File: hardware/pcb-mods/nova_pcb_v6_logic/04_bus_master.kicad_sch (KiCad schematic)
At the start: 5 parts, among them J9 FE-URT-1, U6 Teensy4.1, U7 74HC125

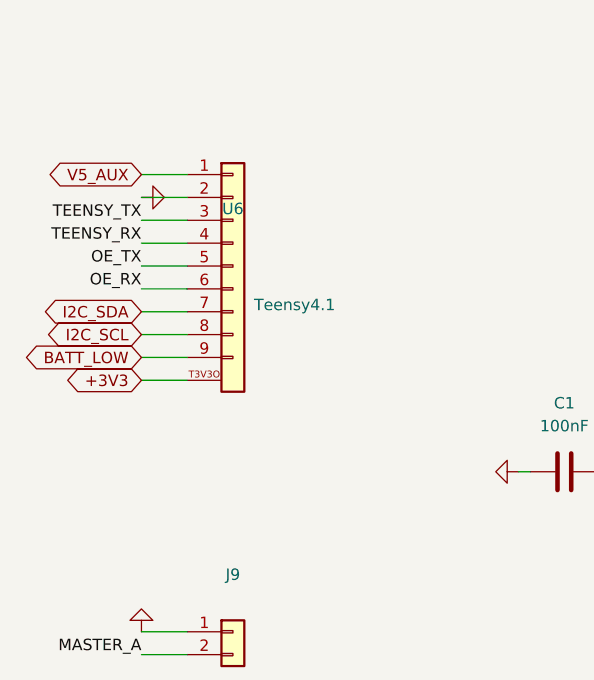
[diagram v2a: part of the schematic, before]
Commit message: logic board: add e-stop sense to Teensy + reconcile firmware pins to board
Hardware e-stop (Q3) killed bucks autonomously but the Teensy was blind —
no ESTOP line crossed J20 (all 12 pins used). Added direct sense so the
SafetyFSM, /estop telemetry, and preflight can see e-stop state.

Board (nova_pcb_v6_logic):
- J21 (Conn_01x02) -> e-stop button 2nd NC dry contact -> Teensy pin 5
  (INPUT_PULLUP) + GND. NC-to-GND = LOW idle; pressed/break/unplug = HIGH
  = e-stop (fail-safe). Dry contact = no level-shift hazard.
- Routed F.Cu J21.1->U6.T5; existing 154 tracks untouched. DRC 0/0.
- Gerbers re-cut. No power-board / J20 change.

Firmware (teensy41_ci green) - pin defines reconciled to board routing
(old defines drove the wrong pins = dead bus):
- bus UART Serial2(7/8) -> Serial1(0/1)
- OE_TX/OE_RX 6/5 -> 2/3
- BATTERY_LOW 3 -> 4
- ESTOP 2 -> 5, polarity LOW->HIGH (NC fail-safe)
- I2C 18/19 unchanged (already matched)
SafetyFSM already latches e-stop until /safety_clear, so snap-back on
release is covered without an inference latch.

Co-Authored-By: Claude Opus 4.8 <noreply@anthropic.com>
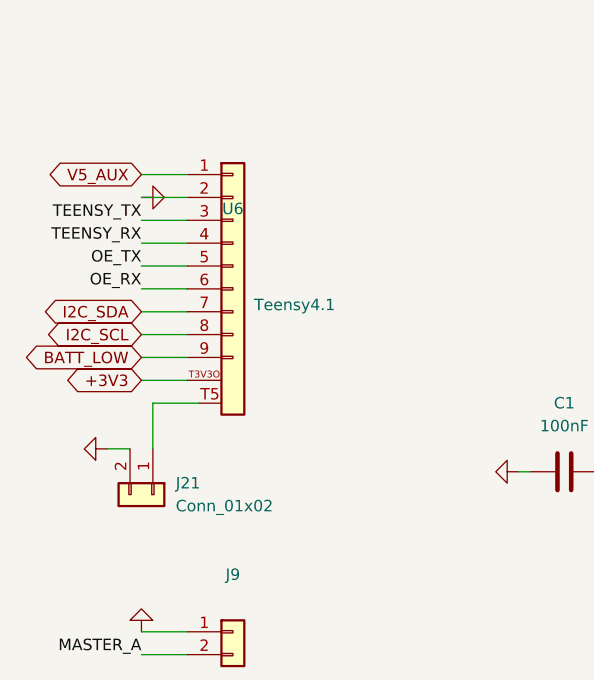
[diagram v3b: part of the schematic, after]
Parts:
- added J21: Conn_01x02, Connector_PinHeader_2.54mm:PinHeader_1x02_P2.54mm_Vertical, symbol Connector_Generic:Conn_01x02
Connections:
- net GND: now also J21.2 (Pin_2)
- new net: J21.1 (Pin_1), U6.T5
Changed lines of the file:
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@@
+	(wire
+		(pts
+			(xy 35.56 96.52) (xy 35.56 91.44)
+		)
+		(stroke
+			(width 0)
+			(type default)
+		)
+	)
 	(wire
 		(pts
@@
 	(wire
 		(pts
+			(xy 30.48 96.52) (xy 33.02 96.52)
+		)
+		(stroke
+			(width 0)
+			(type default)
+		)
+	)
+	(wire
+		(pts
 			(xy 76.2 99.06) (xy 77.47 99.06)
 		)
@@
 		(pts
 			(xy 114.3 57.15) (xy 114.3 62.23)
+		)
+		(stroke
+			(width 0)
+			(type default)
+		)
+	)
+	(wire
+		(pts
+			(xy 35.56 91.44) (xy 40.64 91.44)
 		)
 		(stroke
@@
 		)
 		(pin "T3V3O"
+		)
+		(pin "T5"
 		)
 		(instances
@@
 	)
 	(symbol
+		(lib_id "power:GND")
+		(at 30.48 96.52 270)
+		(unit 1)
+		(exclude_from_sim no)
+		(in_bom yes)
+		(on_board yes)
+		(dnp no)
+		(property "Reference" "#PWR02"
+			(at 30.48 102.87 270)
+			(effects
+				(font
+					(size 1.27 1.27)
+				)
+				(hide yes)
+			)
+		)
+		(property "Value" "GND"
+			(at 30.48 90.17 270)
+			(effects
+				(font
+					(size 1.27 1.27)
+				)
+				(hide yes)
+			)
+		)
+		(property "Footprint" ""
+			(at 30.48 96.52 0)
+			(effects
+				(font
+					(size 1.27 1.27)
+				)
+				(hide yes)
+			)
+		)
+		(property "Datasheet" "~"
+			(at 30.48 96.52 0)
+			(effects
+				(font
+					(size 1.27 1.27)
+				)
+				(hide yes)
+			)
+		)
+		(property "Description" ""
+			(at 30.48 96.52 0)
+			(effects
+				(font
+					(size 1.27 1.27)
+				)
+			)
+		)
+		(pin "1"
+		)
+		(instances
+			(project "nova_pcb_v6_logic"
+				(path "/f535083b-f621-4317-a378-cf746e7f972b/e76e40d6-be2f-49cd-bcdb-1dc94bab9b30"
+					(reference "#PWR02")
+					(unit 1)
+				)
+			)
+		)
+	)
+	(symbol
 		(lib_id "74xx:74LS125")
 		(at 115.57 105.41 0)
@@
 					(unit 1)
 				)
+			)
+		)
+	)
+	(symbol
+		(lib_id "Connector_Generic:Conn_01x02")
+		(at 35.56 101.6 270)
+		(unit 1)
+		(exclude_from_sim no)
+		(in_bom yes)
+		(on_board yes)
+		(dnp no)
+		(fields_autoplaced yes)
+		(property "Reference" "J21"
+			(at 38.1 100.3299 90)
+			(effects
+				(font
+					(size 1.27 1.27)
+				)
+				(justify left)
+			)
+		)
+		(property "Value" "Conn_01x02"
+			(at 38.1 102.8699 90)
+			(effects
+				(font
+					(size 1.27 1.27)
+				)
+				(justify left)
+			)
+		)
+		(property "Footprint" "Connector_PinHeader_2.54mm:PinHeader_1x02_P2.54mm_Vertical"
+			(at 35.56 101.6 0)
+			(effects
+				(font
+					(size 1.27 1.27)
+				)
+				(hide yes)
+			)
+		)
+		(property "Datasheet" "~"
+			(at 35.56 101.6 0)
+			(effects
+				(font
+					(size 1.27 1.27)
+				)
+				(hide yes)
+			)
+		)
+		(property "Description" "Generic connector, single row, 01x02, script generated (kicad-library-utils/schlib/autogen/connector/)"
+			(at 35.56 101.6 0)
+			(effects
+				(font
+					(size 1.27 1.27)
+				)
+				(hide yes)
+			)
+		)
+		(pin "1"
+		)
+		(pin "2"
+		)
+		(instances
+			(project ""
+				(path "/f535083b-f621-4317-a378-cf746e7f972b/e76e40d6-be2f-49cd-bcdb-1dc94bab9b30"
+					(reference "J21")
+					(unit 1)
+				)

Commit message: logic board: U7 -> SN74LVC125A (5V-tolerant) + R7 bus idle pull-up
Full-review findings from the servo-bus level analysis:

U7: 74HC125 -> SN74LVC125A. The 74HC125 at +3V3 is NOT 5V-tolerant
(input abs-max VCC+0.5=3.8V); the STS3215 bus is 5V-TTL, so the servo's
response would over-drive gate2's input (clamp current ~54mA through R1's
22ohm). LVC125A is a drop-in SOIC-14, VCC 3.3V (max 3.6V), 5V-tolerant
inputs, 3.3V outputs (Teensy-safe) -> correct whether bus is 3.3V or 5V.
Value-only change (was stale "74LS125" in sch / "74HC125" in pcb; both
wrong for a 3.3V rail), no reroute. Unified all 5 U7 units + pcb value.

R7 = 10k bus idle pull-up (BUS_SIGNAL -> +3V3). Half-duplex push-pull bus
floats in TX/RX turnaround; R7 holds idle HIGH. Added incrementally
(footprint + 2 hand-routed nets) without disturbing the 154 existing
tracks/pours. Routed pad1->U7.10 (+3V3), pad2 down-and-around below U7 to
the BUS_SIGNAL run (staying clear of the MASTER_A diagonal).

Both boards DRC 0/0. Logic ERC = same known items (no new). Gerbers re-cut.
BOM: order SN74LVC125AD + 10k 0603. Firmware unchanged (hardware-only).

Co-Authored-By: Claude Opus 4.8 <noreply@anthropic.com>
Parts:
- U7: value 74HC125 -> 74LVC125
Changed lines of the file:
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@@
 			)
 		)
-		(property "Value" "74HC125"
+		(property "Value" "74LVC125"
 			(at 114.3 82.55 0)
 			(effects
@@
 			)
 		)
-		(property "Value" "74HC125"
+		(property "Value" "74LVC125"
 			(at 114.3 57.15 0)
 			(effects
@@
 			)
 		)
-		(property "Value" "74HC125"
+		(property "Value" "74LVC125"
 			(at 114.3 138.43 0)
 			(effects
@@
 			)
 		)
-		(property "Value" "74HC125"
+		(property "Value" "74LVC125"
 			(at 115.57 111.76 0)
 			(effects
@@
 			)
 		)
-		(property "Value" "74HC125"
+		(property "Value" "74LVC125"
 			(at 152.4 57.15 0)
 			(effects
